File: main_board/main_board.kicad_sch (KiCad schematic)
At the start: 84 parts, among them J1 Screw_Terminal_01x03, J2 Conn, J3 Screw_Terminal_01x02, J4 Screw_Terminal_01x02, J5 SPI, J6 UPDI, J7 EARTH JUMPER, P1 IEC320-C6, SW1 RESET, SW2 DISP. MODE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

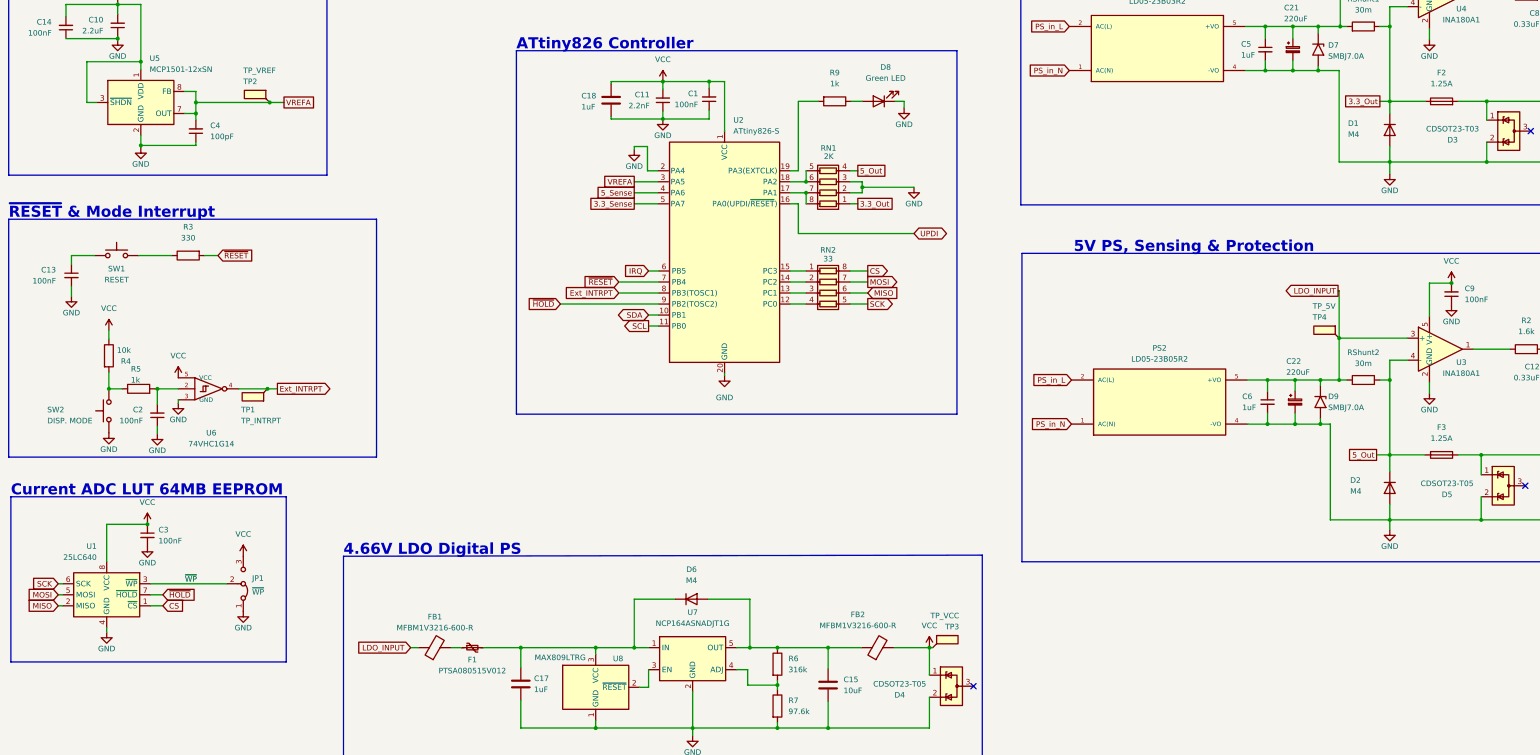
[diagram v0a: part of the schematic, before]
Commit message: Added initial code base, improved and fixed hardware up to Rev 1.5/1.2 for the main and display boards respectively, and add pictures of (mostly) complete result
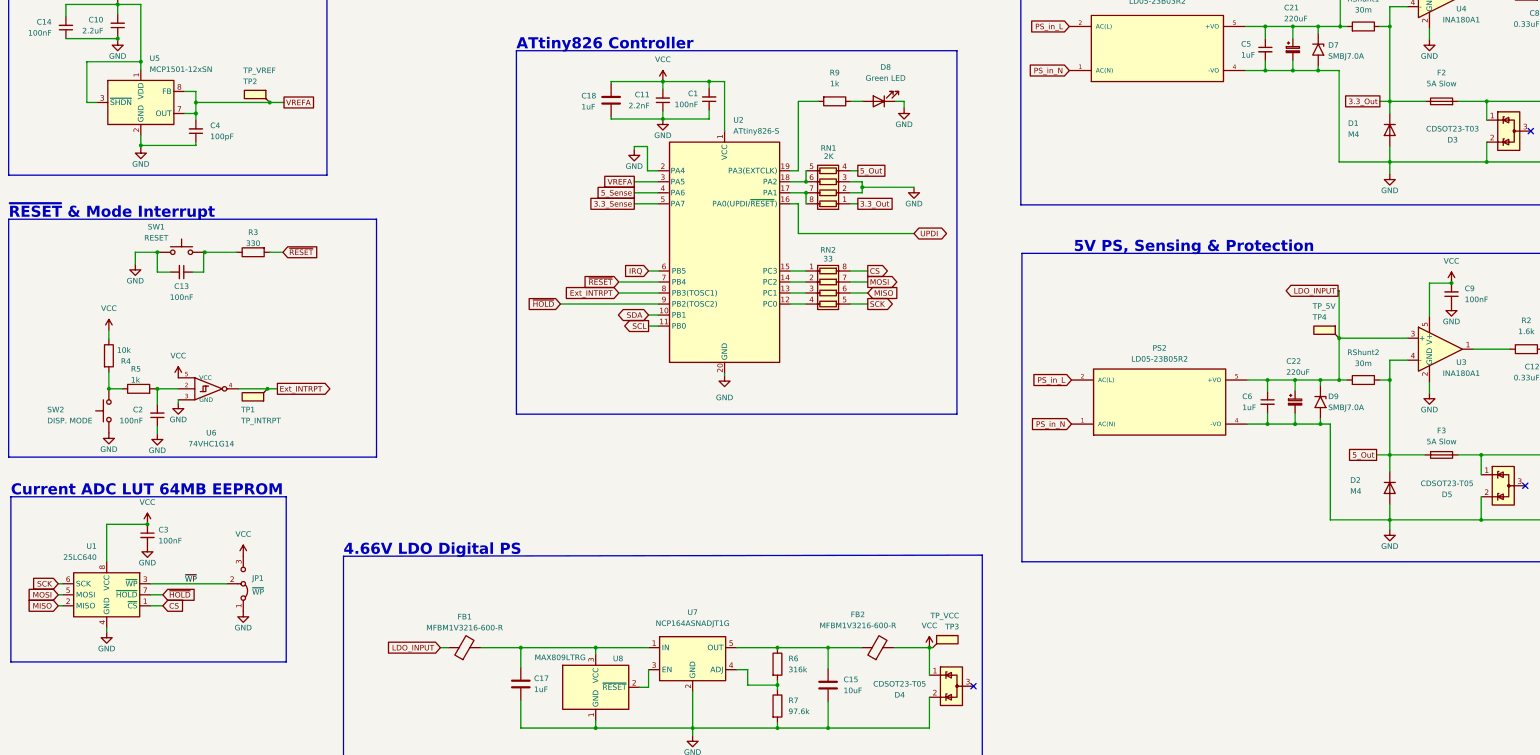
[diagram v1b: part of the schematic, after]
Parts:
- removed D6: M4, Diode_SMD:D_SMB, symbol Device:D
- removed F1: PTSA080515V012, Fuse:Fuse_0805_2012Metric_Pad1.15x1.40mm_HandSolder, symbol Device:Polyfuse_Small
- F2, F3: value 1.25A -> 5A Slow
- J2: footprint personal:DISPIO10 -> Connector_PinHeader_2.54mm:PinHeader_2x05_P2.54mm_Vertical
- J7: footprint Connector_PinSocket_2.54mm:PinSocket_1x01_P2.54mm_Vertical -> Connector_PinHeader_2.54mm:PinHeader_1x01_P2.54mm_Vertical
- SW2: footprint Connector_PinSocket_2.54mm:PinSocket_1x02_P2.54mm_Vertical -> Connector_PinHeader_2.54mm:PinHeader_1x02_P2.54mm_Vertical
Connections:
- net GND: now also SW1.1
- net at FB1.2: now also C17.1, U7.1 (IN), U8.3 (VCC)
- net at C13.1: now also R3.1, SW1.2; no longer SW1.1
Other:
- moved on the sheet: C13, FB1, R3, SW1
